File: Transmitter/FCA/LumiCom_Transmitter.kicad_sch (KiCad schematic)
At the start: 38 parts, among them J1 V, J2 IN_B, J3 IN_A, J4 OUT_B, J5 OUT_A, U1 OPA2675

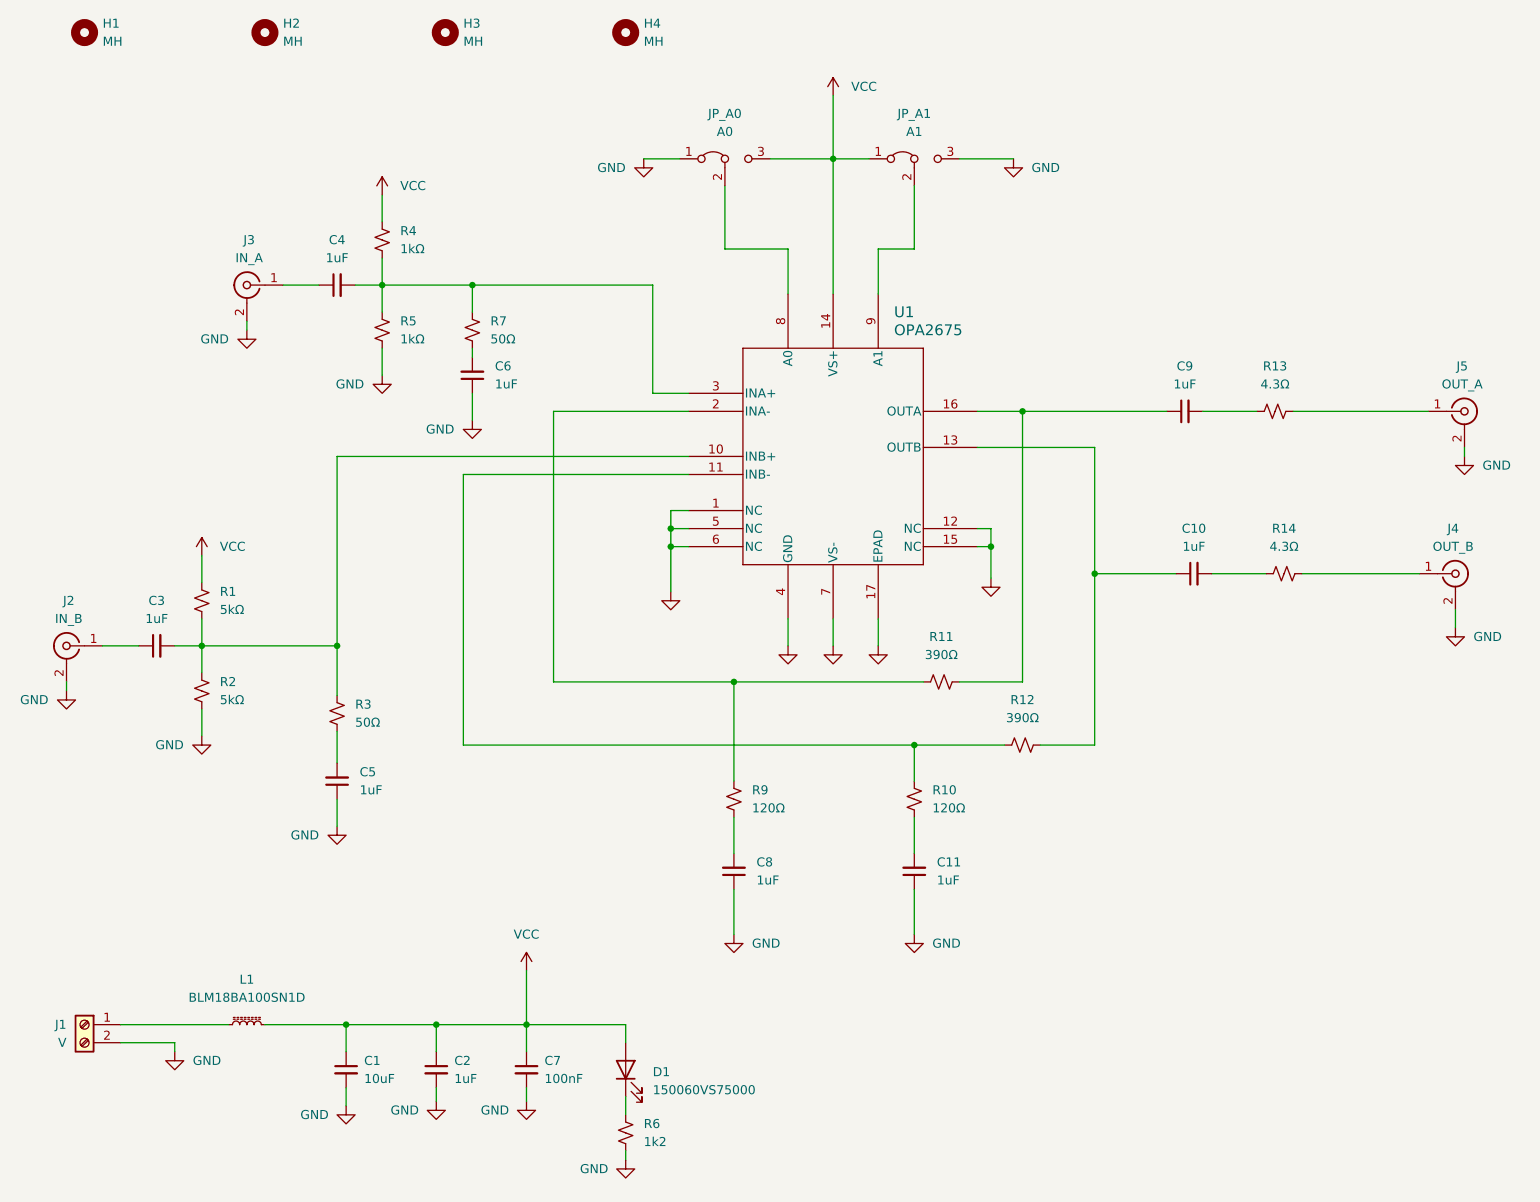
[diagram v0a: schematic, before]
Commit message: Updated FCA symbols
Updated FCA symbols with mouser number parts.
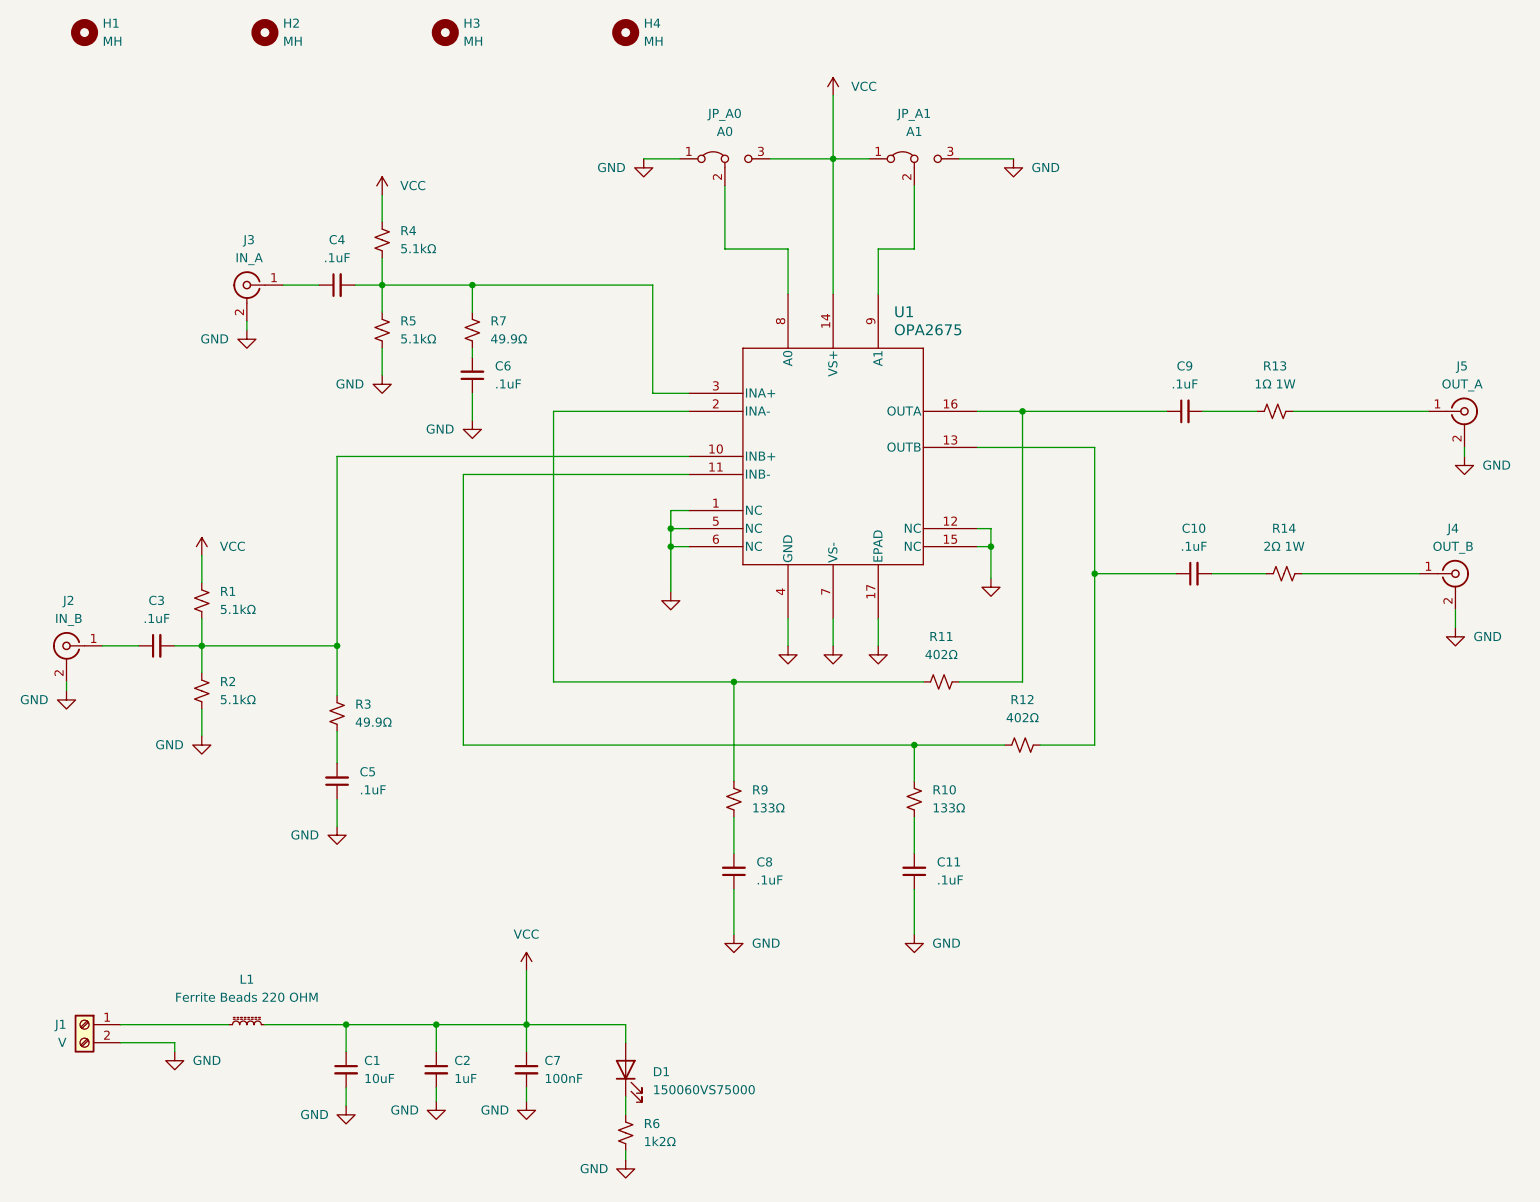
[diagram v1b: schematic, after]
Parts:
- C1: Manufacturer (none) -> Murata Electronics; Manufacturer Part Number (none) -> GRM188Z71A106MA73D; Mouser Part Number (none) -> 81-GRM188Z71A106MA3D
- C10, C9: value 1uF -> .1uF; footprint Capacitor_SMD:C_0603_1608Metric -> Capacitor_SMD:C_0402_1005Metric_Pad0.74x0.62mm_HandSolder; LCSC C14663 -> (none); Manufacturer (none) -> KYOCERA AVX; Manufacturer Part Number (none) -> 530L104KT16; Mouser Part Number (none) -> 581-530L104KT16
- C11, C3, C4, C5, C6, C8: value 1uF -> .1uF; footprint Capacitor_SMD:C_0603_1608Metric -> Capacitor_SMD:C_0402_1005Metric_Pad0.74x0.62mm_HandSolder; LCSC C19702 -> (none); Manufacturer (none) -> KYOCERA AVX; Manufacturer Part Number (none) -> 530L104KT16; Mouser Part Number (none) -> 581-530L104KT16
- C2: Manufacturer (none) -> Samsung Electro-Mechanics; Manufacturer Part Number (none) -> CL10B105KP8NNNC; Mouser Part Number (none) -> 187-CL10B105KP8NNNC
- C7: Manufacturer (none) -> Samsung Electro-Mechanics; Manufacturer Part Number (none) -> CL10B104KO8NFNC; Mouser Part Number (none) -> 187-CL10B104KO8NFNC
- D1: value 150060VS75000 -> 150060VS75000; Manufacturer (none) -> Wurth Elektronik; Manufacturer Part Number (none) -> 150060VS75000; Mouser Part Number (none) -> 710-150060VS75000
- L1: value BLM18BA100SN1D -> Ferrite Beads 220 OHM; Manufacturer (none) -> Murata Electronics; Manufacturer Part Number (none) -> BLM18KG221SN1D; Mouser Part Number (none) -> 81-BLM18KG221SN1D
- R1, R2: value 5kΩ -> 5.1kΩ; LCSC C21190 -> (none); Manufacturer (none) -> Vishay / Dale; Manufacturer Part Number (none) -> CRCW06035K10FKEA; Mouser Part Number (none) -> 71-CRCW0603-5.1K-E3
- R10, R9: value 120Ω -> 133Ω; footprint Resistor_SMD:R_0603_1608Metric -> Resistor_SMD:R_0402_1005Metric_Pad0.72x0.64mm_HandSolder; LCSC C22787 -> (none); Manufacturer (none) -> Bourns; Manufacturer Part Number (none) -> CRT0402-FZ-1330GLF; Mouser Part Number (none) -> 652-CRT0402FZ1330GLF
- R11, R12: value 390Ω -> 402Ω; footprint Resistor_SMD:R_0603_1608Metric -> Resistor_SMD:R_0402_1005Metric_Pad0.72x0.64mm_HandSolder; LCSC C23151 -> (none); Manufacturer (none) -> Bourns; Manufacturer Part Number (none) -> CRT0402-FZ-4020GLF; Mouser Part Number (none) -> 652-CRT0402FZ4020GLF
- R13: value 4.3Ω -> 1Ω 1W; footprint Resistor_SMD:R_1210_3225Metric_Pad1.30x2.65mm_HandSolder -> Resistor_SMD:R_1206_3216Metric_Pad1.30x1.75mm_HandSolder; LCSC C102477 -> (none); Manufacturer (none) -> SEI Stackpole; Manufacturer Part Number (none) -> RNCL1206FT1R00; Mouser Part Number (none) -> 708-RNCL1206FT1R00
- R14: value 4.3Ω -> 2Ω 1W; footprint Resistor_SMD:R_1210_3225Metric_Pad1.30x2.65mm_HandSolder -> Resistor_SMD:R_1206_3216Metric_Pad1.30x1.75mm_HandSolder; LCSC C102477 -> (none); Manufacturer (none) -> SEI Stackpole; Manufacturer Part Number (none) -> RNCL1206FT2R00; Mouser Part Number (none) -> 708-RNCL1206FT2R00
- R3, R7: value 50Ω -> 49.9Ω; LCSC C23185 -> (none); Manufacturer (none) -> Vishay / Beyschlag; Manufacturer Part Number (none) -> MCT06030C4999FP500; Mouser Part Number (none) -> 594-MCT06030C4999FP5
- R4, R5: value 1kΩ -> 5.1kΩ; LCSC C21190 -> (none); Manufacturer (none) -> Vishay / Dale; Manufacturer Part Number (none) -> CRCW06035K10FKEA; Mouser Part Number (none) -> 71-CRCW0603-5.1K-E3
- R6: value 1k2 -> 1k2Ω; Manufacturer (none) -> Vishay / Dale; Manufacturer Part Number (none) -> CRCW08051K20FKEAC; Mouser Part Number (none) -> 71-CRCW08051K20FKEAC
- U1: LCSC C19711669 -> (none); Manufacturer (none) -> Texas Instruments; Manufacturer Part Number (none) -> OPA2675RGVR; Mouser Part Number (none) -> 595-OPA2675RGVR

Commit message: FCA DRC fix
FCA DRC fix
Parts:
- U1: footprint Package_DFN_QFN:Texas_RGV0016A_VQFN-16-1EP_4x4mm_P0.65mm_EP2.1x2.1mm_ThermalVias -> LumiCom_Transmitter:Texas_OPA2675
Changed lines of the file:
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@@
 			)
 		)
-		(property "Footprint" "Package_DFN_QFN:Texas_RGV0016A_VQFN-16-1EP_4x4mm_P0.65mm_EP2.1x2.1mm_ThermalVias"
+		(property "Footprint" "LumiCom_Transmitter:Texas_OPA2675"
 			(at 139.7 67.818 0)
 			(effects

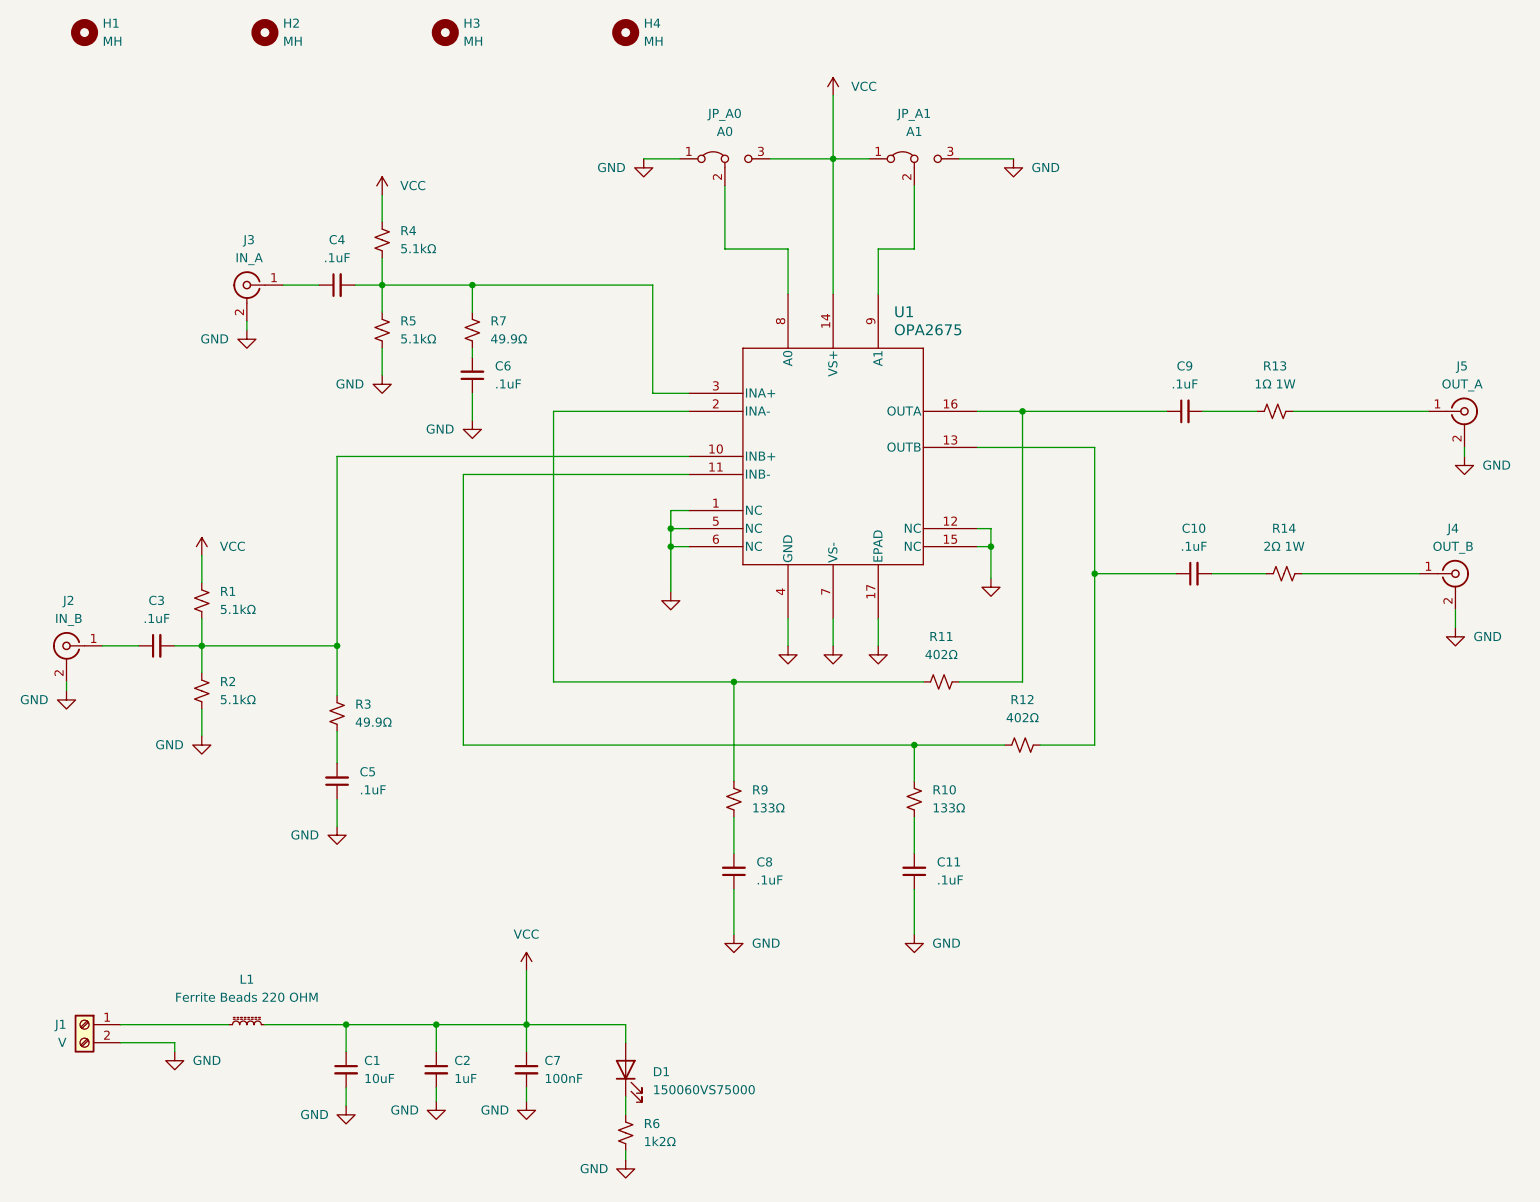
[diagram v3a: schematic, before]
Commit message: FCA fixed
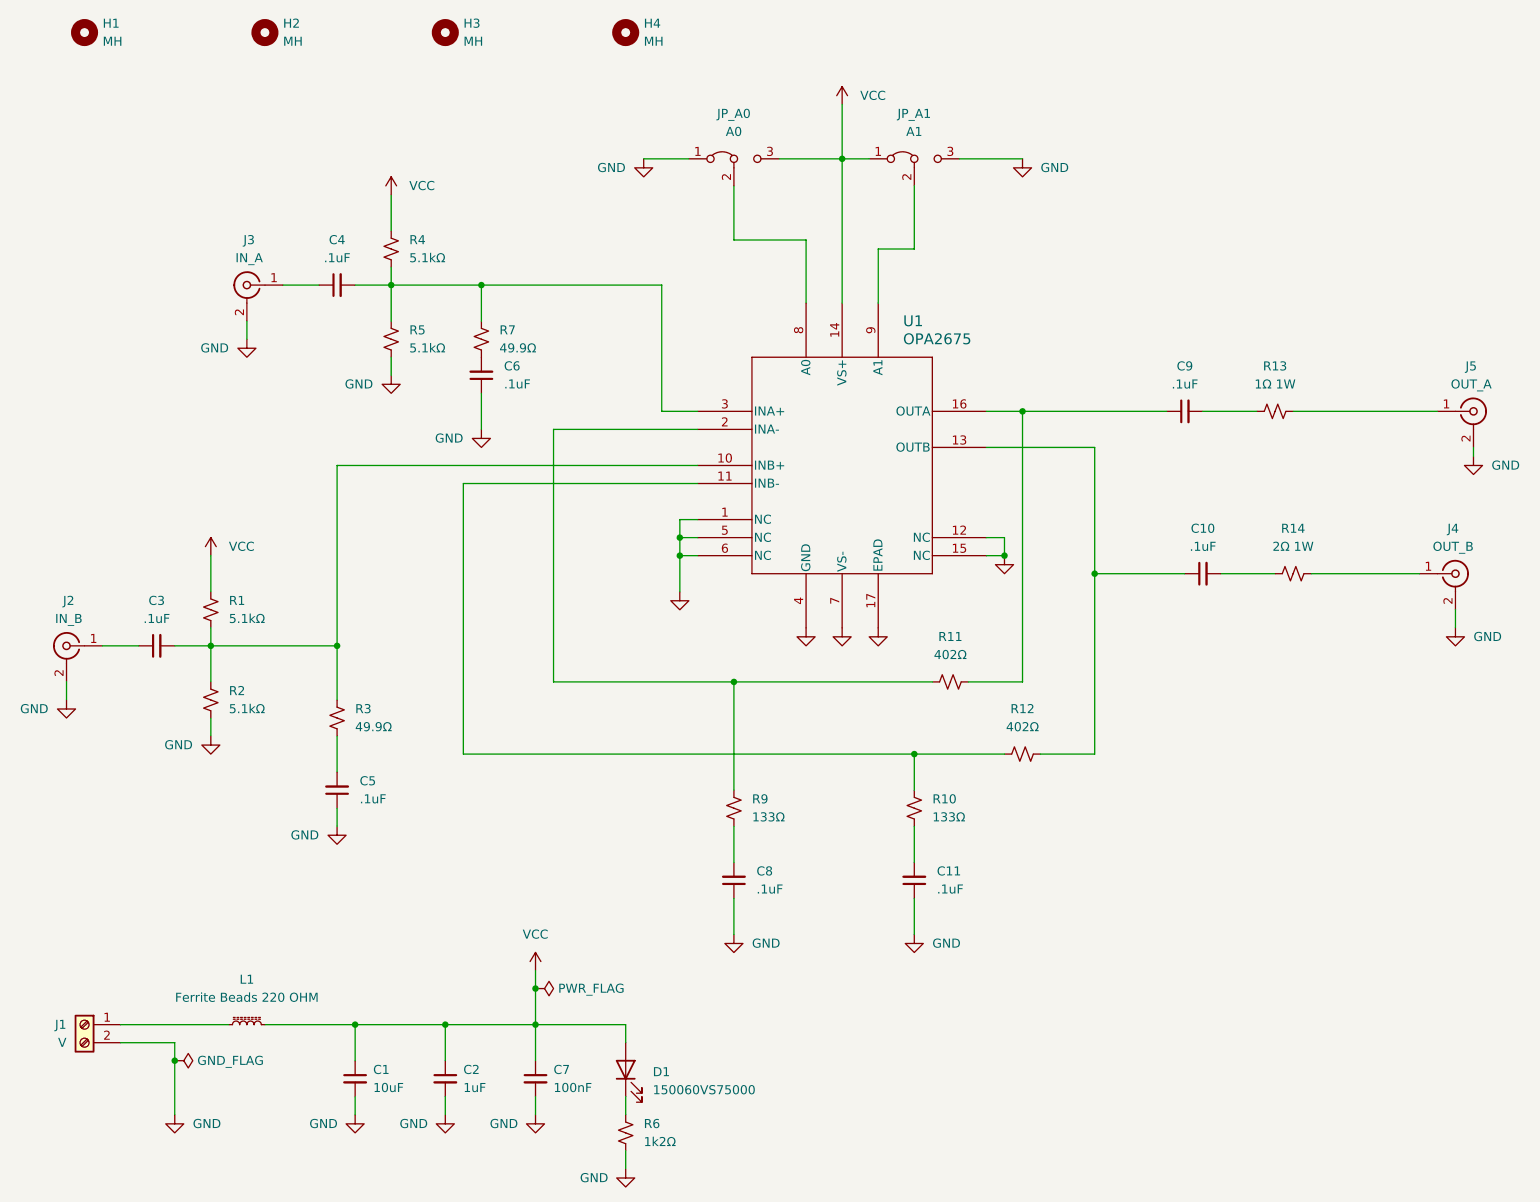
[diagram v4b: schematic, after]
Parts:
- R6: Manufacturer Vishay / Dale -> Vishay / Dale; Manufacturer Part Number CRCW08051K20FKEAC -> CRCW06031K20FKEA; Mouser Part Number 71-CRCW08051K20FKEAC -> 71-CRCW0603-1.2K-E3
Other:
- moved on the sheet: C1, C10, C11, C2, C5, C6, C7, C8, J5, JP_A0, R1, R10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
